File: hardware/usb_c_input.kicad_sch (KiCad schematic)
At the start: 3 parts, among them J7 USB_C_Receptacle_USB2.0_16P, U10 TPD4EUSB30

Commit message: usb_pd_controller: tüm güç zincirini tek A3 sayfasında topla
powergeneration (TPS55340 ön-boost + AOZ1284 buck) ve poweroutput (panel
konnektörleri) blokları bu sayfaya taşındı. Sayfa A2'den A3'e indirildi;
bloklar altı slota yeniden çizildi:
  satır 1: PD kontrolcü + VBUS şönt/anahtar | AP74502Q çıkış anahtarı |
           INA228 ölçüm + panel çıkışı (TVS ve boşaltma direnci dahil)
  satır 2: TPS55340 ön-boost | AOZ1284 buck | I2C seviye dönüştürücü

Okunurluk için: buck bloğu iki satıra bölünüp sütun aralıkları 12.7 mm'ye
çıkarıldı, PD kontrolcüde V5V rayı kapı hattının üstüne alındı, INA228 ile
panel konnektörleri tek blokta birleşti, V_PRE artık ön-boost çıkışından
buck girişine gerçek telle gidiyor.

Boş kalan sayfalar silindi: powergeneration, poweroutput, powersensing,
calc_usb_pd_controller, CALC_MCU, CALC_USB_C_INPUT (sayfa sembolleri ve
gopo.kicad_pro kayıtları dahil). Şematik 12 sayfadan 6 sayfaya indi.

Bağlantılar isimden bağımsız karşılaştırmayla doğrulandı: kayıp/yeni net
yok; yalnızca sayfa kapsamı değişen 9 net yeniden adlandı
(/POWER GENERATION/* -> /USB_PD_CONTROLLER/*). ERC değişmedi
(0 hata, 2 eski uyarı), lint temiz.

Co-Authored-By: Claude Opus 5 <noreply@anthropic.com>
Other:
- removed sheet CALC_USB_C_INPUT
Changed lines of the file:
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@@
-		)
-	)
-	(sheet
-		(at 17.78 184.15)
-		(size 12.7 5.08)
-		(exclude_from_sim no)
-		(in_bom yes)
-		(on_board yes)
-		(dnp no)
-		(fields_autoplaced yes)
-		(stroke
-			(width 0.1524)
-			(type solid)
-		)
-		(fill
-			(color 255 61 254 1)
-		)
-		(property "Sheetname" "CALC_USB_C_INPUT"
-			(at 17.78 183.4384 0)
-			(show_name no)
-			(do_not_autoplace no)
-			(effects
-				(font
-					(size 1.27 1.27)
-				)
-				(justify left bottom)
-			)
-		)
-		(property "Sheetfile" "CALC_USB_C_INPUT.kicad_sch"
-			(at 17.78 189.8146 0)
-			(show_name no)
-			(do_not_autoplace no)
-			(effects
-				(font
-					(size 1.27 1.27)
-				)
-				(justify left top)
-			)
-		)
-		(instances
-			(project "gopo"
-				(path "/a43081a6-9aa2-4898-9347-bbcb5849dafd/b1c77f87-da4f-471e-9ed3-42007402a7f4"
-					(page "10")
-				)
-			)
-			(project "usb_c_input"
-				(path "/0ea5422e-f571-4c4e-a341-b9d41b5fb49d"
-					(page "2")
-				)
-			)
 		)
 	)

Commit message: hardware: komponent alanlarını standarda oturt, yalnız Value+Reference göster
134 komponentin alan seti design_decisions/standards/komponent-field-standardi.csv
uyarınca yeniden kuruldu (3.144 alan). Her komponent grup koduna atandı ve ALL +
gruba özel alanlar standarttaki sırayla yazıldı; CSV'de koşullu işaretli alanlar
(Sadece Zener / Sadece ADC / Sadece RTC) yalnız ilgili parçaya kondu.

Eski alan adları standarda birleşti: Manufacturer Part Number ve DisplayMPN ->
MPN, Voltage -> VoltageRating, Field5 -> DesignNote / TerminationStyle,
Supplier + Battery -> SelectionNote / DesignNote. Sim.* alanları korundu.

Value IEC 60062 koduna çevrildi (10 kΩ/4,7k/100K/10kR karışıktı -> 10k/4k7/100k).
Value'dan çıkan gerilim, güç, tolerans ve dielektrik kendi alanlarına taşındı.
L1 ve D2'de Value MPN'di; parametrik değere çevrilip sipariş kodu MPN'e alındı.

Görünürlük tek kurala indi: yalnız Reference + Value. Description 119 sembolde
açıktı, kapandı. Güç sembolleri depo kuralına oturdu (Reference gizli, GND ve
PWR_FLAG değeri gizli, +3.3V görünür).

Parça verisi gerektiren 1.755 alan TBD bırakıldı; yalnız depodan (footprint,
lib_id, BOM_PRELIMINARY, tasarım notları) doğrulanabilen değerler yazıldı,
MPN veya datasheet parametresi uydurulmadı.

Okunabilirlik: C3 değeri PD_VBUS_SENSED telinin üstündeydi, TP5 referansı
PD_GATE etiketiyle çakışıyordu; ikisinin de yalnız metin konumu kaydırıldı.

gopo.kicad_pro'ya 10 çekirdek alanın Field Name Templates kaydı eklendi.

Bu commit ayrıca KiCad 10'un kendi kaydını taşır: güç sembollerinden
(fields_autoplaced no) düştü ve C4/TP4 elle boş alana taşındı.

Doğrulama: netlist farkı YOK, ERC 2 uyarı (değişmedi), lint 6/1/0/0 (değişmedi),
field_geometry farkı yalnız C3 ve TP5.

Co-Authored-By: Claude Opus 5 <noreply@anthropic.com>
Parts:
- D3: AssemblyNote (none) -> TBD; BreakdownVoltage (none) -> TBD; Capacitance (none) -> TBD; Category (none) -> Circuit Protection; ChannelCount (none) -> 1; ClampingVoltage (none) -> TBD; DesignNote (none) -> TBD; Height (none) -> TBD; Lifecycle (none) -> TBD; MPN (none) -> SMBJ30A; Manufacturer (none) -> TBD; MountingType (none) -> Surface Mount; OperatingTemp (none) -> TBD; Package (none) -> SMB (DO-214AA); PeakPulseCurrent (none) -> TBD; Polarity (none) -> Unidirectional; RoHS (none) -> TBD; SelectionNote (none) -> TBD; StandoffVoltage (none) -> 30V; Subcategory (none) -> TVS Diodes
- J7: AssemblyNote (none) -> TBD; CCPinsPresent (none) -> Yes; Category (none) -> Connectors, Interconnects; ConnectorType (none) -> Receptacle; ContactPlating (none) -> TBD; CurrentRating (none) -> TBD; DesignNote (none) -> TBD; Height (none) -> TBD; Lifecycle (none) -> TBD; MPN (none) -> USB4105-GF-A; Manufacturer Part Number USB4105-GF-A -> (none); MatingCycles (none) -> TBD; MountingType (none) -> Surface Mount; OperatingTemp (none) -> TBD; Orientation (none) -> Right Angle; Package (none) -> USB-C 16P Top Mount Horizontal; Pitch (none) -> 0.5mm; PositionCount (none) -> 16; PowerRating (none) -> TBD; RoHS (none) -> TBD; RowCount (none) -> 2; SBUPins (none) -> TBD; SelectionNote (none) -> TBD; Series (none) -> TBD; ShellType (none) -> Top Mount; Shielding (none) -> TBD; Subcategory (none) -> USB, DVI, HDMI Connectors; USBVersion (none) -> USB 2.0 Type-C; VoltageRating (none) -> TBD
- U10: AssemblyNote (none) -> TBD; BreakdownVoltage (none) -> TBD; Capacitance (none) -> TBD; Category (none) -> Circuit Protection; ChannelCount (none) -> 4; ClampingVoltage (none) -> TBD; DesignNote (none) -> USB2.0 veri hatti ESD dizisi.; Height (none) -> TBD; Lifecycle (none) -> TBD; MPN (none) -> TPD4EUSB30; Manufacturer (none) -> Texas Instruments; MountingType (none) -> Surface Mount; OperatingTemp (none) -> TBD; Package (none) -> USON-10 (2.5x1.0mm); PeakPulseCurrent (none) -> TBD; Polarity (none) -> Unidirectional; RoHS (none) -> TBD; SelectionNote (none) -> TBD; StandoffVoltage (none) -> TBD; Subcategory (none) -> TVS Diodes

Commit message: hardware: RTC'yi BQ32000 + süper kapasitöre geçir, Özdisan BOM'unu şemaya aktar
RTC (mcu):
- U4 RV-3028-C7 -> BQ32000DR (SOIC-8, I2C 0x68, open-drain IRQ, dahili
  trickle charger). Y1 ABS25-32.768KHZ-T (CL 12,5 pF, harici yük C yok),
  C33 Korchip DCL5R5155HF 1,5 F/5,5 V (H-tipi yatay coin, ~22 gün yedek).
- BT1 (CR2032), R22, R23, C10 kaldırıldı; C9 100n -> 1u0 (datasheet >= 1 uF).
- Yeni footprint: Power_Output_Custom:Korchip_DCL_H-Type_D19.0mm_P20.00mm_Horizontal
  (Korchip DCL datasheet çiziminden; numune ile doğrulanmalı).
- Beklenen netlist farkı yalnız RTC netleri: RTC_SCL/SDA/INT U4 pin
  numaraları, Net-(U4-OSCI/OSCO/VBACK) yeni; Net-(BT1-+), Net-(U4-EVI),
  Net-(U4-VBACKUP), U4 CLKOUT kalktı. ERC değişmedi (0 hata, 2 eski uyarı).

Özdisan BOM aktarımı (tüm sayfalar):
- MPN, Manufacturer, parametrik alanlar ve SelectionNote (Özdisan kodu,
  stok 21.09.2026, durum) BOM_OZDISAN_REV_C_20260921.xlsx'ten yazıldı.
- Onaylı değişiklikler: C5/C20/C21 0805; C8/C12/C13/C25/C27/C28 4u7 50V
  X7R 1210; C15/C29 47u 35V hibrit (Device:C_Polarized, CP_Elec_6.3x5.8);
  C31 0603 25V; R59 0805 1/3W; R40 3k24 + R39 10k2 (VOUT 3,3185 V);
  U6 TL431AIDBZR; D4 SX36.
- Stokta olmayan parçalarda (U1, U2, U7, U8, U10, U12, L1, L2, C19) MPN
  korundu, öneri SelectionNote ve todo.txt'de. Alan geometrisi ve
  görünürlük değişmedi. PCB şemadan henüz güncellenmedi.

Aynı commit'te önceden commit edilmemiş çalışma: Q3/Q5 SQJB60EP ve U3
INA226 entegrasyonu, raporları ve datasheet'leri.

Co-Authored-By: Claude Opus 5 <noreply@anthropic.com>
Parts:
- D3: MPN SMBJ30A -> SMBJ30A-E3/52; Manufacturer TBD -> Vishay; SelectionNote TBD -> Özdisan 507320; stok 15956 (21.09.2026); Uygun. Şema açıkla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
- J7: SelectionNote TBD -> Özdisan 955183; stok 93 (21.09.2026); Uygun. 21.09 üçüncü t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
- U10: SelectionNote TBD -> Özdisan (21.09.2026): Stokta yok. Stokta yok. Stoktaki TPD4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
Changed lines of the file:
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@@
 			)
 		)
-		(property "SelectionNote" "TBD"
+		(property "SelectionNote" "Özdisan (21.09.2026): Stokta yok. Stokta yok. Stoktaki TPD4E1U06DBVR / TPD4E001DBVR SOT-23-6 kılıflı; kullanmak footprint değişikliği gerektirir."
 			(at 156.21 115.57 0)
 			(hide yes)
@@
 			)
 		)
-		(property "SelectionNote" "TBD"
+		(property "SelectionNote" "Özdisan 955183; stok 93 (21.09.2026); Uygun. 21.09 üçüncü tur: USB konnektör kategorisi indekslendi; tasarımdaki parçanın kendisi stokta (93). Muadil gerekirse: GCT USB4110-GF-A (223 stok, farklı footprint), KLS L-KLS1-5409-L2-01-R 16P (425 stok) — 5A akım değeri ve footprint doğrulanmalı."
 			(at 102.87 91.44 0)
 			(hide yes)
@@
 			)
 		)
-		(property "Manufacturer" "TBD"
-			(at 210.82 118.11 0)
-			(hide yes)
-			(show_name no)
-			(do_not_autoplace no)
-			(effects
-				(font
-					(size 1.27 1.27)
-				)
-			)
-		)
-		(property "MPN" "SMBJ30A"
+		(property "Manufacturer" "Vishay"
+			(at 210.82 118.11 0)
+			(hide yes)
+			(show_name no)
+			(do_not_autoplace no)
+			(effects
+				(font
+					(size 1.27 1.27)
+				)
+			)
+		)
+		(property "MPN" "SMBJ30A-E3/52"
 			(at 210.82 118.11 0)
 			(hide yes)
@@
 			)
 		)
-		(property "SelectionNote" "TBD"
-			(at 210.82 118.11 0)
-			(hide yes)
+		(property "SelectionNote" "Özdisan 507320; stok 15956 (21.09.2026); Uygun. Şema açıklaması '400W / SMA' diyor ama footprint SMB; SMB/600W parça footprint'e uyar."
+			(at 210.82 118.11 0)
+			(hide yes)

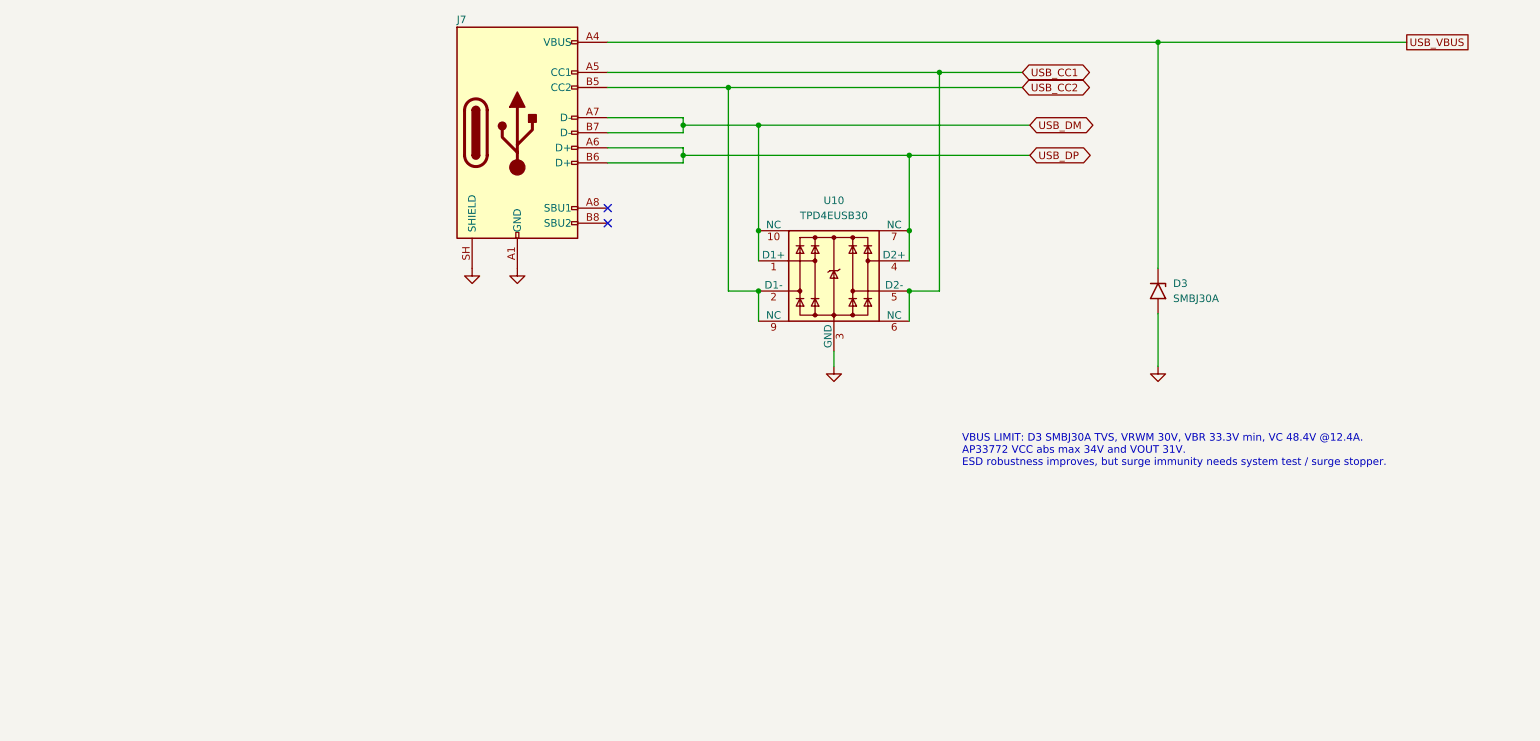
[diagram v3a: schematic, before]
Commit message: hardware: çıkış anahtarını LM74801'e geçir, USB-C korumasını ve OUT_EN'i düzelt
Çıkış anahtarı / ters akım (usb_pd_controller):
- U12 AP74502Q -> LM74801-Q1 (LM74801QDRRRQ1, WSON-12, EP boşta). AP74502Q
  ideal diyot değil; çıkış açıkken ters akım doğrudan adaptör VBUS'ına
  gidiyordu. Ortak-source Q5: HGATE -> Q5A (GATE_DRV, R54/C30, D6),
  DGATE -> Q5B (yeni net), A/OUT = SRC_COMMON, C = SW_OUT, VS/VSNS/SW = V_PRE.
- R55 232k -> 237k: LM74801 OV 30.4 V (29.5-31.3 V), 28 V EPR +%5 üstünde.
- OUT_EN kapatamıyordu (EN ~1.57 V > 1.32 V): R57 kalktı, U13 74LVC1G08
  (SN74LVC1G08DBVR) EN = OUT_EN AND ~ALERT; R61 4k7 OUT_EN pull-down, C35.
- AOZ1284 kompanzasyonu: R41 12k7 -> 51k, C19 18n -> 15n (fC ~5 -> ~20 kHz).
- Q3/Q5 footprint: yeni Package_SO_Custom:Vishay_PowerPAK_SO-8L_Dual
  (Vishay doc 63817'den ölçüldü; 6/8 yalnız bakır eş drain pedleri).
- TL431DBZ önbelleği KiCad 10 kütüphanesinden yenilendi (pin uçları aynı).

MCU:
- RTC (BQ32000) PD/INA226 I2C bus'ına alındı, R25/R26 kalktı; OUT_EN = GPIO6
  (MTCK), GPIO7 boş.

USB-C girişi (usb_c_input):
- CC1/CC2'ye Rd 5k1 (R62/R63) eklendi; AP33772S Figure 1 harici Rd istiyor,
  şemada hiç yoktu.
- CC1/CC2 5.5 V'luk U10'dan ayrıldı (AP33772S CC 34 V'a dayanır, U10 28 V
  kısa devrede yanardı); D8/D9 SMF30A CC ESD opsiyonu DNP.
- U10 TPD4EUSB30 -> USBLC6-2SC6 (yalnız D+/D-, jumper_pin_groups ile
  flow-through, VBUS pini +3.3V). D3 SMBJ30A yer için sağa taşındı.

Doğrulama: her adımda beklenen netlist farkı; son durum ERC 0 hata / 0 uyarı,
101 net. Parçalar Özdisan stoğundan (SelectionNote alanlarında).

Kayıtlar:
- todo.txt açık kalanlara göre yeniden düzenlendi.
- design_decisions/output/SEMA_TAMAMLANAN_TODO_REV_C_20260922.md: bu
  maddelerin gerekçe ve hesapları.
- design_decisions/output/CIKIS_GERILIMI_28V_TAVANI_20260922.md: 28 V tavanı.
- Datasheet'ler: LM7480-Q1, SMF (Thinking), USBLC6-2.

Co-Authored-By: Claude Opus 5 <noreply@anthropic.com>
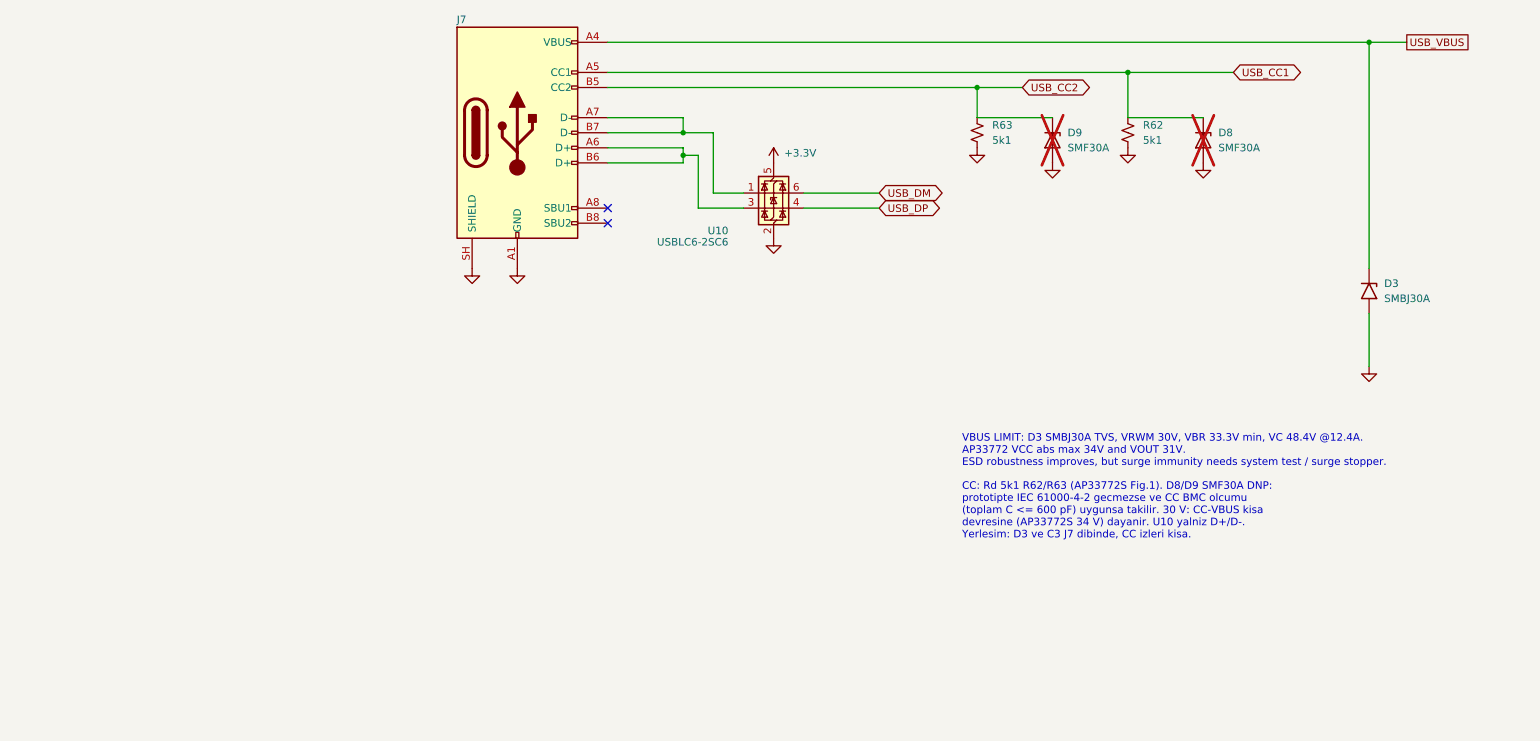
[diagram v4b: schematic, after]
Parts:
- added D8, D9: SMF30A, Diode_SMD:D_SOD-123F, symbol Device:D_Zener
- added R62, R63: 5k1, Resistor_SMD:R_0402_1005Metric, symbol Device:R_Small_US
- D3: BreakdownVoltage TBD -> 33.3V min; ClampingVoltage TBD -> 48.4V @12.4A; PeakPulseCurrent TBD -> 12.4A
- U10: value TPD4EUSB30 -> USBLC6-2SC6; footprint Package_SON:USON-10_2.5x1.0mm_P0.5mm -> Package_TO_SOT_SMD:SOT-23-6; symbol Power_Protection:TPD4EUSB30 -> Power_Path_Custom:USBLC6-2SC6; Capacitance TBD -> 3.5pF max; ChannelCount 4 -> 2; DesignNote USB2.0 veri hatti ESD dizisi. -> Yalniz D+/D- (flow-through 1-6, 3-4). VBUS pini +3.3V: USB_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; MPN TPD4EUSB30 -> USBLC6-2SC6; Manufacturer Texas Instruments -> STMicroelectronics; Package USON-10 (2.5x1.0mm) -> SOT-23-6; SelectionNote Özdisan (21.09.2026): Stokta yok. Stokta yok. Stoktaki TPD4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 -> Özdisan 402751; stok 7375 (22.09.2026); Uygun. TPD4EUSB30 s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; StandoffVoltage TBD -> 5.25V
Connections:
- net GND: now also U10.2 (GND), D8.2 (A), D9.2 (A), R62.2, R63.2; no longer U10.3 (GND), U10.8 (GND)
- net USB_CC1: now also D8.1 (K), R62.1; no longer U10.5 (D2-), U10.6 (NC)
- net USB_CC2: now also D9.1 (K), R63.1; no longer U10.2 (D1-), U10.9 (NC)
- net USB_DM: now also U10.6 (I/O1); no longer J7.A7 (D-), J7.B7 (D-), U10.1 (D1+), U10.10 (NC)
- net USB_DP: no longer J7.A6 (D+), J7.B6 (D+), U10.7 (NC)
- new net: J7.A7 (D-), J7.B7 (D-), U10.1 (I/O1)
- new net: J7.A6 (D+), J7.B6 (D+), U10.3 (I/O2)
- new net +3.3V: U10.5 (VBUS)
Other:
- note added: "CC: Rd 5k1 R62/R63 (AP33772S Fig.1). D8/D9 SMF30A DNP: prototipte IEC 61000-4-2 gecmezse ve CC BMC olcumu (toplam C <= 600 pF) uygunsa takilir. 30 V: CC-VBUS kisa devresine (AP33772S 34 V) dayanir. U10 yalniz D+/D-. Yerlesim: D3 ve C3 J7 dibinde, CC izleri kisa."
- moved on the sheet: D3
